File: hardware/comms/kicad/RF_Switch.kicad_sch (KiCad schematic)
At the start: 13 parts, among them Y1 25MHz, Y2 Si5351A-B-GT

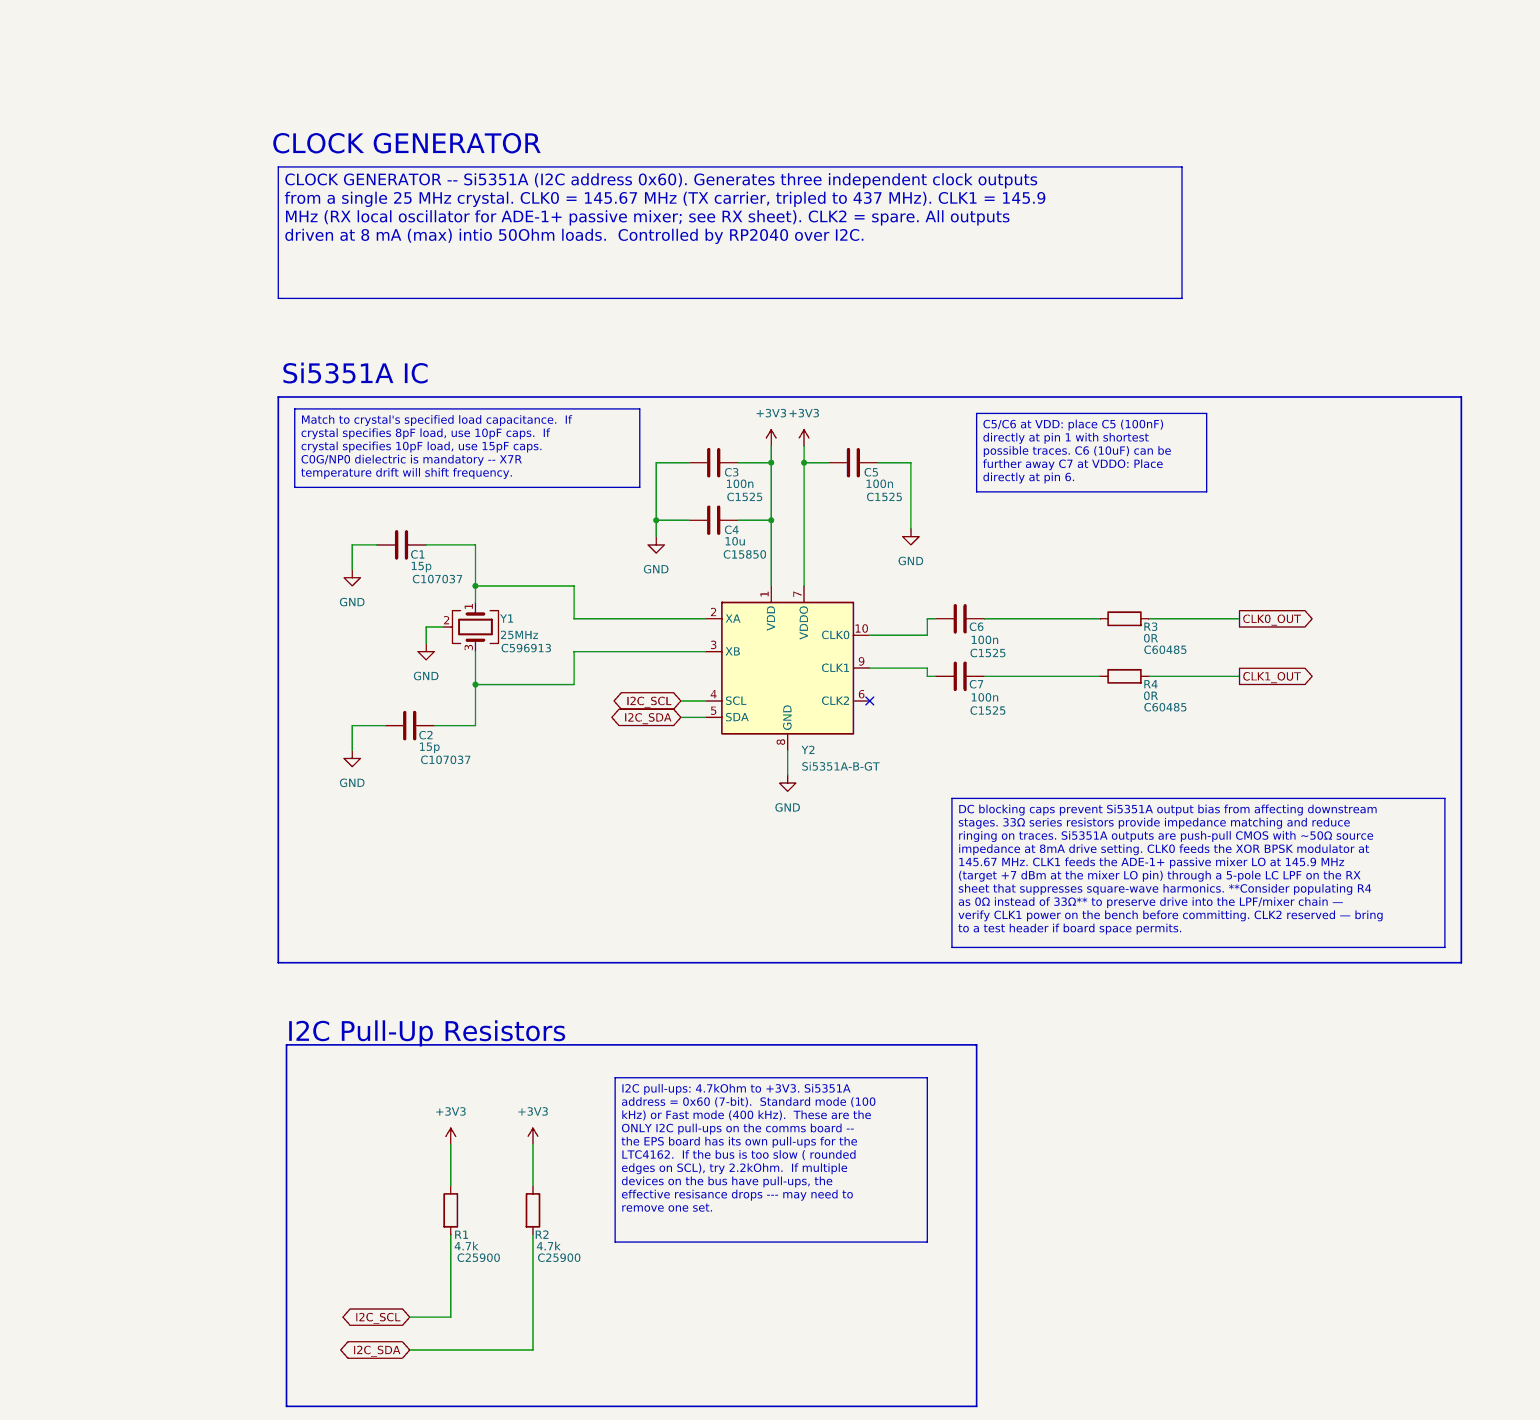
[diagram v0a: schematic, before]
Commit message: Checkpoint validated single-antenna comms routing before placement optimization
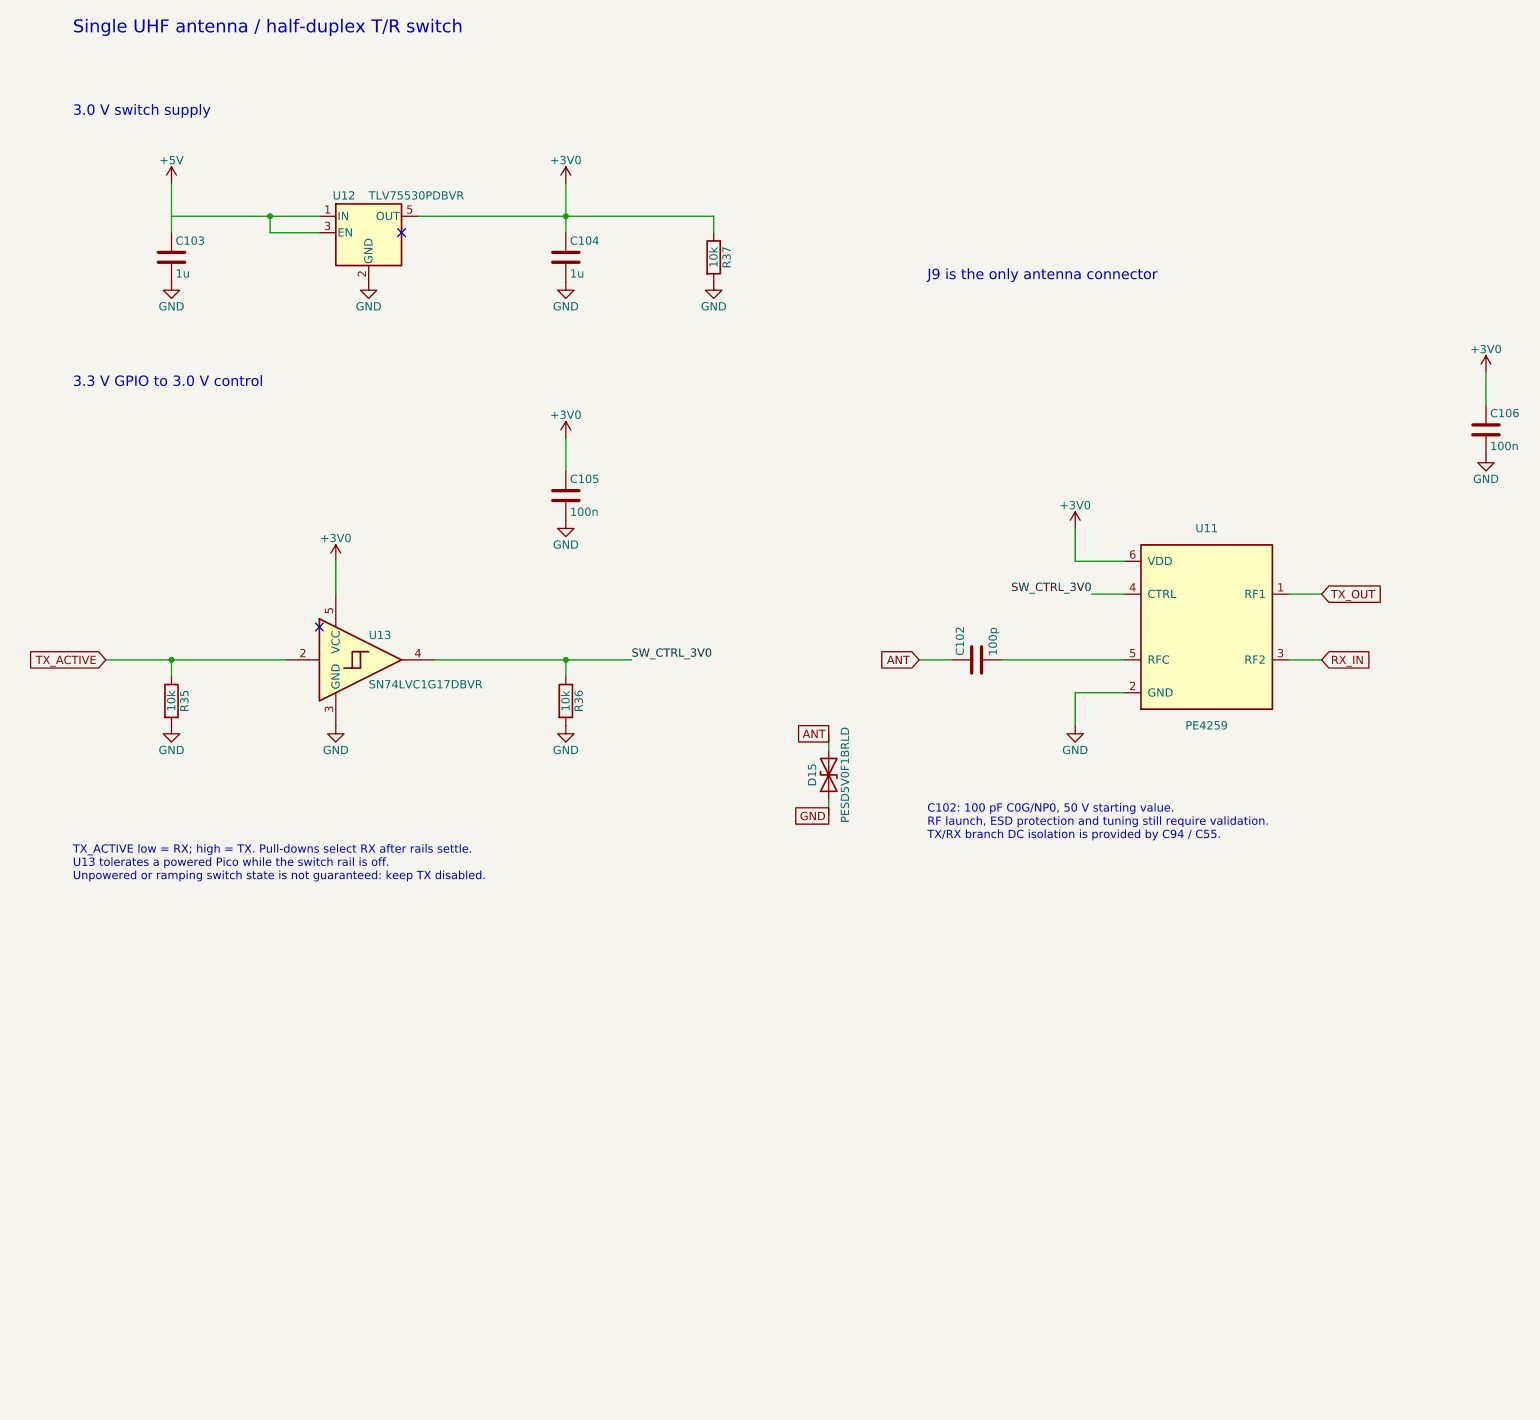
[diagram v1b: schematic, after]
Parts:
- removed C1, C2: 15p, Capacitor_SMD:C_0603_1608Metric, symbol Device:C
- removed C3, C5, C6, C7: 100n, Capacitor_SMD:C_0402_1005Metric, symbol Device:C
- removed C4: 10u, Capacitor_SMD:C_0805_2012Metric, symbol Device:C
- removed R1, R2: 4.7k, Resistor_SMD:R_0402_1005Metric, symbol Device:R
- removed R3, R4: 0R, Resistor_SMD:R_0402_1005Metric, symbol Device:R
- removed Y1: 25MHz, Crystal:Crystal_SMD_3225-4Pin_3.2x2.5mm, symbol Device:Crystal_GND24
- removed Y2: Si5351A-B-GT, Package_SO:MSOP-10_3x3mm_P0.5mm, symbol Oscillator:Si5351A-B-GT
- added C102: 100p, Capacitor_SMD:C_0402_1005Metric, symbol Device:C
- added C103, C104: 1u, Capacitor_SMD:C_0603_1608Metric, symbol Device:C
- added C105, C106: 100n, Capacitor_SMD:C_0402_1005Metric, symbol Device:C
- added D15: PESD5V0F1BRLD, Diode_SMD:D_SOD-882D, symbol Device:D_TVS
- added R35, R36, R37: 10k, Resistor_SMD:R_0402_1005Metric, symbol Device:R
- added U11: PE4259, Package_TO_SOT_SMD:SOT-363_SC-70-6, symbol Ember_RF:PE4259
- added U12: TLV75530PDBVR, Package_TO_SOT_SMD:SOT-23-5, symbol Regulator_Linear:TLV75530PDBV
- added U13: SN74LVC1G17DBVR, Package_TO_SOT_SMD:SOT-23-5, symbol 74xGxx:74LVC1G17
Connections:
- net GND: now also C103.2, C104.2, C105.2, C106.2, D15.1 (A1), R35.2, R36.2, R37.2, U11.2 (GND), U12.2 (GND), U13.3 (GND)
- new net: C102.2, U11.5 (RFC)
- new net +3V0: C104.1, C105.1, C106.1, R37.1, U11.6 (VDD), U12.5 (OUT), U13.5 (VCC)
- new net +5V: C103.1, U12.1 (IN), U12.3 (EN)
- new net ANT: C102.1, D15.2 (A2)
- new net RX_IN: U11.3 (RF2)
- new net SW_CTRL_3V0: R36.1, U11.4 (CTRL), U13.4
- new net TX_ACTIVE: R35.1, U13.2
- new net TX_OUT: U11.1 (RF1)
- no-connect marks 1 -> 2
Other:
- note added: "3.0 V switch supply"
- note added: "3.3 V GPIO to 3.0 V control"
- note added: "C102: 100 pF C0G/NP0, 50 V starting value. RF launch, ESD protection and tuning still require validation. TX/RX branch DC isolation is provided by C94 / C55."
- note added: "J9 is the only antenna connector"
- note added: "Single UHF antenna / half-duplex T/R switch"
- note added: "TX_ACTIVE low = RX; high = TX. Pull-downs select RX after rails settle. U13 tolerates a powered Pico while the switch rail is off. Unpowered or ramping switch state is not guaranteed: keep TX disabled."
- note removed: "CLOCK GENERATOR"
- note removed: "I2C Pull-Up Resistors"
- note removed: "Si5351A IC"
- title: CubeSat Comms -- Clock Generator -> (none)

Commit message: progress on comms board
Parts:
- C102: LCSC Part # (none) -> C1546; Manufacturer Part # (none) -> 0402CG101J500NT
- C103, C104: LCSC Part # (none) -> C29936; Manufacturer Part # (none) -> CL10B105KA8NNNC; Voltage 16V -> 25V
- C105, C106: LCSC Part # (none) -> C1525; Manufacturer Part # (none) -> CL05B104KO5NNNC
- R35, R36, R37: LCSC Part # (none) -> C25744; Manufacturer Part # (none) -> 0402WGF1002TCE
- U11: LCSC Part # (none) -> C470892; Manufacturer Part # (none) -> PE4259-63
- U12: LCSC Part # (none) -> C507268; Manufacturer Part # (none) -> TLV75530PDBVR
- U13: LCSC Part # (none) -> C7836; Manufacturer Part # (none) -> SN74LVC1G17DBVR
